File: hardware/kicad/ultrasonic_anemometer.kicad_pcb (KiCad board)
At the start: 2 copper layers, 24 parts, among them P1 CONN_01X06, U1 LM1117-3.3, U2 MCP6294, U3 DSPIC33EP512GP504, Y1 8MHz

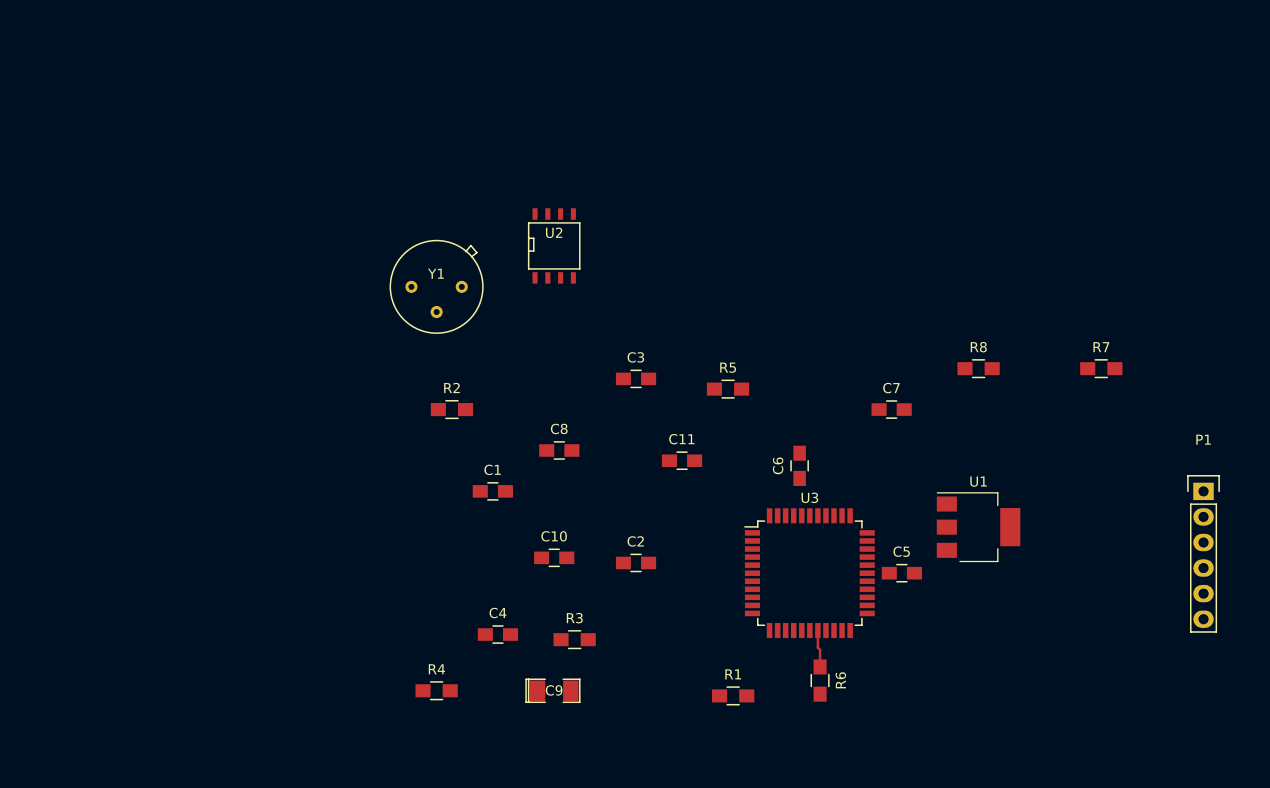
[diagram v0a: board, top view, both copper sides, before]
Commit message: Updated schematic and PCB. Added OPAMP to the Modex library.
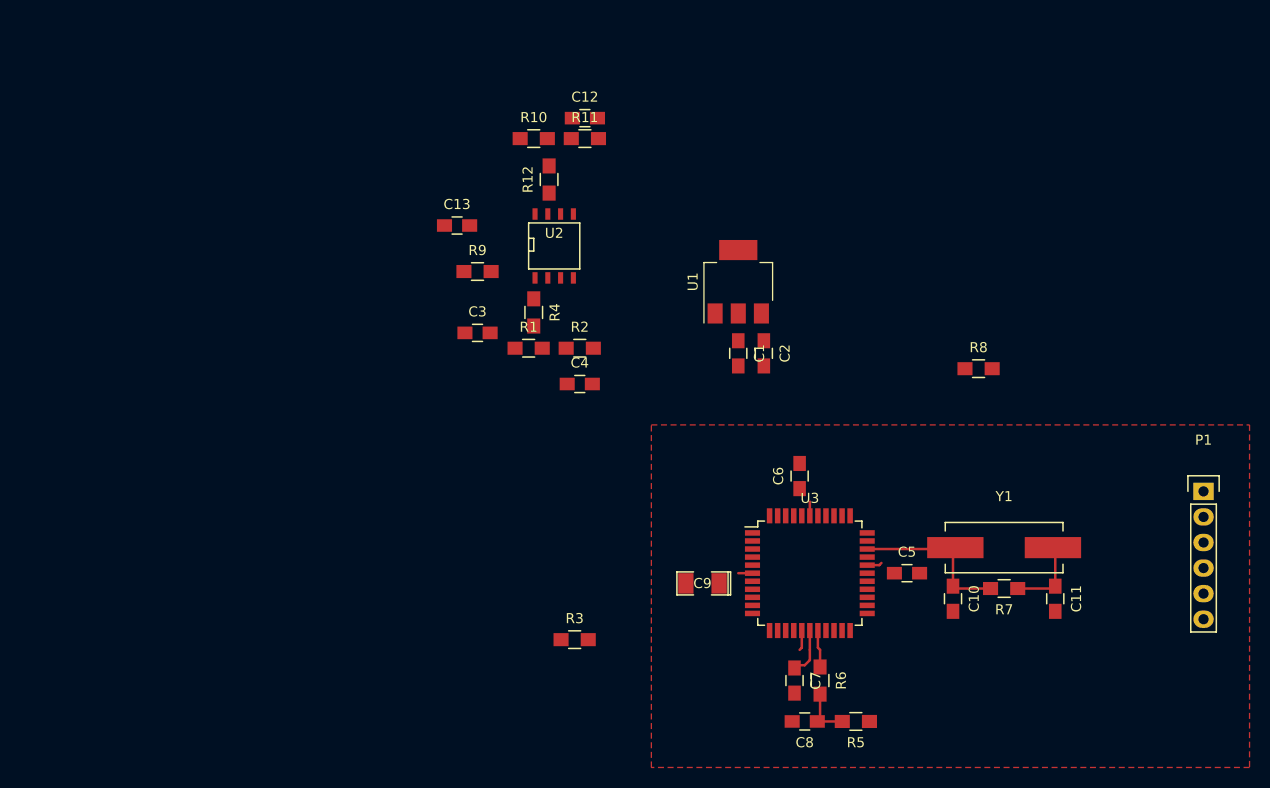
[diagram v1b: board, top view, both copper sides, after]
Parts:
- added C12: 100n, Capacitors_SMD:C_0805_HandSoldering, F.Cu at (125.5, 63.5)
- added C13: C, Capacitors_SMD:C_0805_HandSoldering, F.Cu at (112.8, 74.2)
- added R10: 360k, Resistors_SMD:R_0805_HandSoldering, F.Cu at (120.4, 65.5)
- added R11: 360k, Resistors_SMD:R_0805_HandSoldering, F.Cu at (125.5, 65.5)
- added R12: 180k, Resistors_SMD:R_0805_HandSoldering, F.Cu at (121.9, 69.6)
- added R9: 10k, Resistors_SMD:R_0805_HandSoldering, F.Cu at (114.8, 78.7)
- C4: value C -> 100n
- R1, R2: value R -> 360k
- R3: value R -> 10k
- R4: value R -> 180k
- U2: value MCP6294 -> MCP6492
- Y1: footprint Crystals:Crystal_HC35-U -> Crystals:Crystal_HC49-SD_SMD
- moved Y1 62.1 mm to (167.1, 106.2)
- moved R1 40.1 mm to (119.9, 86.4)
- moved C10 39.8 mm to (162.1, 111.3), turned to 270 degrees
- moved C11 39.5 mm to (172.2, 111.3), turned to 270 degrees
- moved R4 38.8 mm to (120.4, 82.8), turned to 270 degrees
- moved C8 36.3 mm to (147.3, 123.4), turned to 180 degrees
- moved R5 35.4 mm to (152.4, 123.4), turned to 180 degrees
- moved U1 34.1 mm to (140.7, 79.8), turned to 90 degrees
- moved C7 28.6 mm to (146.3, 119.4), turned to 270 degrees
- moved C1 28.0 mm to (140.7, 86.9), turned to 270 degrees
- moved C4 26.2 mm to (125.0, 89.9)
- moved C2 24.4 mm to (143.3, 86.9), turned to 270 degrees
- moved R7 23.9 mm to (167.1, 110.2), turned to 180 degrees
- moved C9 18.2 mm to (137.2, 109.7), turned to 180 degrees
- moved C3 16.4 mm to (114.8, 84.8)
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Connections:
- C1 pad 1: Net-(C1-Pad1) -> /Digital/p3v3
- C1 pad 2: Net-(C1-Pad2) -> GND
- C2 pad 2: Net-(C2-Pad2) -> GND
- R3 pad 1: Net-(R3-Pad1) -> Net-(C3-Pad2)
- R3 pad 2: Net-(C3-Pad1) -> Net-(R3-Pad2)
- R4 pad 2: Net-(R3-Pad1) -> Net-(C3-Pad1)
- U1 pad 1: Net-(U1-Pad1) -> GND
- U1 pad 2: Net-(U1-Pad2) -> /Digital/p3v3
- U1 pad 3: Net-(U1-Pad3) -> Net-(C2-Pad1)
- U1 pad 4: Net-(U1-Pad2) -> /Digital/p3v3
- U2 pad 1: Net-(U2-Pad1) -> Net-(R4-Pad1)
- U2 pad 2: Net-(U2-Pad2) -> Net-(C3-Pad1)
- U2 pad 3: Net-(U2-Pad3) -> Net-(C4-Pad1)
- U2 pad 4: +5V -> GND
- U2 pad 8: Net-(R4-Pad1) -> +5V
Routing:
- net Net-(C10-Pad1): track 0.00 -> 16.6 mm
- net Net-(C11-Pad1): track 0.00 -> 7.75 mm
- net GND: track 0.00 -> 6.33 mm
- net /Digital/MCLR: track 0.00 -> 5.31 mm
- net Net-(C7-Pad1): track 0.00 -> 4.78 mm
- added copper zone on F.Cu, net GND

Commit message: Updated schematic and PCB.
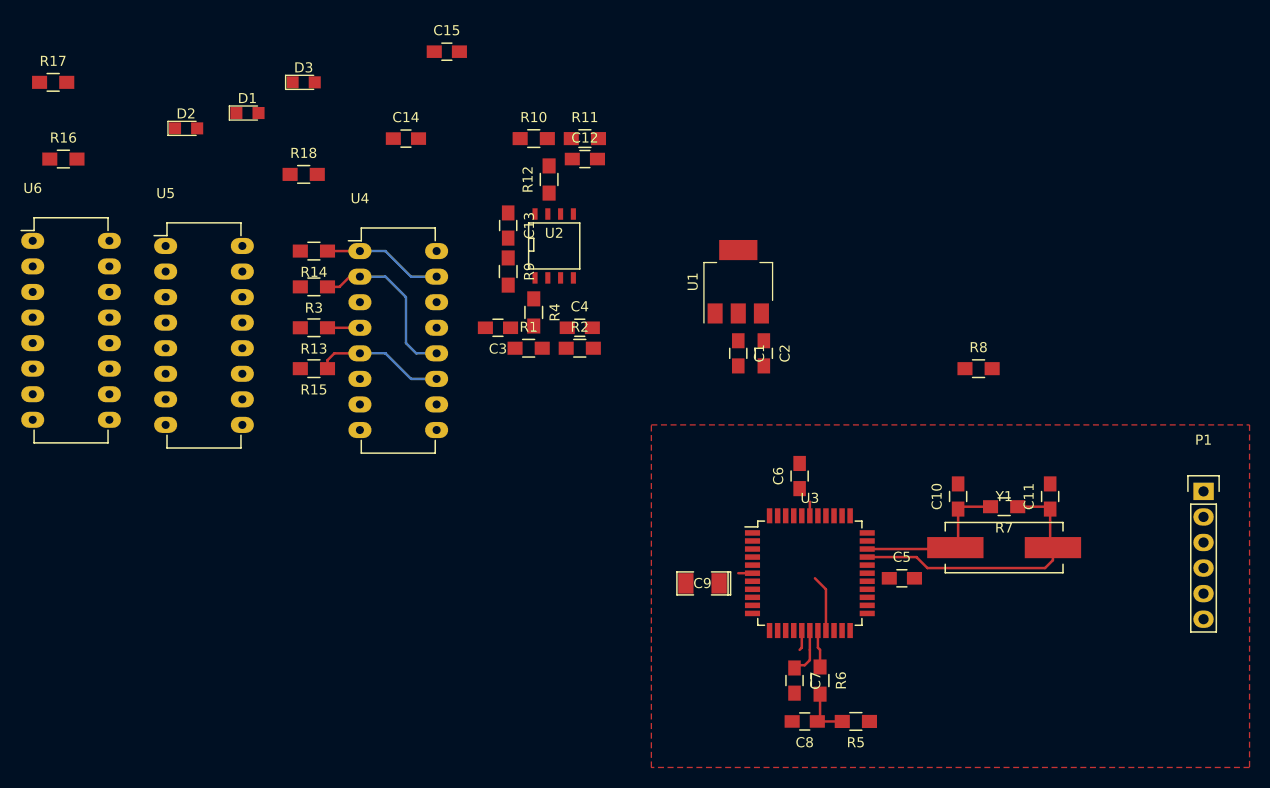
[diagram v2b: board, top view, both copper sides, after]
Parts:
- added C14: np, Capacitors_SMD:C_0805_HandSoldering, F.Cu at (107.7, 65.5)
- added C15: np, Capacitors_SMD:C_0805_HandSoldering, F.Cu at (111.8, 56.9)
- added D1: LED, LEDs:LED_0805, F.Cu at (91.9, 63.0)
- added D2: LED, LEDs:LED_0805, F.Cu at (85.9, 64.5)
- added D3: LED, LEDs:LED_0805, F.Cu at (97.5, 59.9)
- added R13: 10k, Resistors_SMD:R_0805_HandSoldering, F.Cu at (98.6, 84.3)
- added R14: 10k, Resistors_SMD:R_0805_HandSoldering, F.Cu at (98.6, 76.7)
- added R15: 10k, Resistors_SMD:R_0805_HandSoldering, F.Cu at (98.6, 88.4)
- added R16: 100, Resistors_SMD:R_0805_HandSoldering, F.Cu at (73.7, 67.6)
- added R17: 100, Resistors_SMD:R_0805_HandSoldering, F.Cu at (72.6, 59.9)
- added R18: 100, Resistors_SMD:R_0805_HandSoldering, F.Cu at (97.5, 69.1)
- added U4: 4052, Housings_DIP:DIP-16_W7.62mm_LongPads, F.Cu at (103.1, 76.7)
- added U5: 74LS368, Housings_DIP:DIP-16_W7.62mm_LongPads, F.Cu at (83.8, 76.2)
- added U6: 74LS368, Housings_DIP:DIP-16_W7.62mm_LongPads, F.Cu at (70.6, 75.7)
- Y1: value 8MHz -> 10.24 MHz
- moved R3 43.6 mm to (98.6, 80.3), turned to 180 degrees
- moved C10 10.2 mm to (162.6, 101.1), turned to 90 degrees
- moved C11 10.2 mm to (171.7, 101.1), turned to 90 degrees
- moved R7 8.13 mm to (167.1, 102.1)
- moved C4 5.59 mm to (125.0, 84.3)
- moved C13 5.08 mm to (117.9, 74.2), turned to 270 degrees
- moved C12 4.06 mm to (125.5, 67.6)
- moved R9 3.05 mm to (117.9, 78.7), turned to 270 degrees
- moved C3 2.09 mm to (116.8, 84.3), turned to 180 degrees
- moved C5 0.72 mm to (157.0, 109.2)
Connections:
- R12 pad 1: Net-(R12-Pad1) -> /Analog/ADC
- R3 pad 1: Net-(C3-Pad2) -> Net-(R3-Pad1)
- U2 pad 7: Net-(R12-Pad1) -> /Analog/ADC
- U3 pad 19: Net-(U3-Pad19) -> /Analog/ADC
- U3 pad 2: Net-(U3-Pad2) -> /Digital/RUN
- U3 pad 3: Net-(U3-Pad3) -> /Digital/ERROR
- U3 pad 4: Net-(U3-Pad4) -> /Digital/OK
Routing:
- net Net-(C11-Pad1): track 7.75 -> 28.1 mm
- net Net-(R3-Pad1): track 0.00 -> 17.1 mm
- net Net-(R15-Pad1): track 0.00 -> 13.0 mm
- net Net-(R14-Pad1): track 0.00 -> 11.9 mm
- net /Analog/ADC: track 0.00 -> 5.64 mm
- net Net-(R13-Pad1): track 0.00 -> 3.22 mm
- net GND: track 6.33 -> 4.83 mm
